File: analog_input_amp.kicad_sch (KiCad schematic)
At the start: 29 parts, among them U301 THS4521ID

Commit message: PCB: WIP Schematic: minor changes (decoupling, logic element ordering)
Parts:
- C304: value 100n -> 1u; Mfr PN CL21B104KBFNNNE -> CL21B105KOFNNNG
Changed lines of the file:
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@@
+    (pin "2")
+  )
+  (symbol (lib_id "Device:C") (at 101.6 158.75 0) (unit 1)
+    (in_bom yes) (on_board yes) (fields_autoplaced)
+    (property "Reference" "C304" (id 0) (at 104.521 157.9153 0)
+      (effects (font (size 1.27 1.27)) (justify left))
+    )
+    (property "Value" "1u" (id 1) (at 104.521 160.4522 0)
+      (effects (font (size 1.27 1.27)) (justify left))
+    )
+    (property "Footprint" "Capacitor_SMD:C_0805_2012Metric" (id 2) (at 102.5652 162.56 0)
+      (effects (font (size 1.27 1.27)) hide)
+    )
+    (property "Datasheet" "~" (id 3) (at 101.6 158.75 0)
+      (effects (font (size 1.27 1.27)) hide)
+    )
+    (property "Spec1" "" (id 4) (at 101.6 158.75 0)
+      (effects (font (size 1.27 1.27)) hide)
+    )
+    (property "Spec2" "" (id 5) (at 101.6 158.75 0)
+      (effects (font (size 1.27 1.27)) hide)
+    )
+    (property "Tolerance" "" (id 6) (at 101.6 158.75 0)
+      (effects (font (size 1.27 1.27)) hide)
+    )
+    (property "Mfr" "Samsung" (id 7) (at 101.6 158.75 0)
+      (effects (font (size 1.27 1.27)) hide)
+    )
+    (property "Mfr PN" "CL21B105KOFNNNG" (id 8) (at 101.6 158.75 0)
+      (effects (font (size 1.27 1.27)) hide)
+    )
+    (pin "1")
     (pin "2")
   )
@@
       (effects (font (size 1.27 1.27)) hide)
     )
-    (pin "1")
-    (pin "2")
-  )
-  (symbol (lib_id "Device:C") (at 101.6 158.75 0) (unit 1)
-    (in_bom yes) (on_board yes) (fields_autoplaced)
-    (property "Reference" "C304" (id 0) (at 104.521 157.9153 0)
-      (effects (font (size 1.27 1.27)) (justify left))
-    )
-    (property "Value" "100n" (id 1) (at 104.521 160.4522 0)
-      (effects (font (size 1.27 1.27)) (justify left))
-    )
-    (property "Footprint" "Capacitor_SMD:C_0805_2012Metric" (id 2) (at 102.5652 162.56 0)
-      (effects (font (size 1.27 1.27)) hide)
-    )
-    (property "Datasheet" "~" (id 3) (at 101.6 158.75 0)
-      (effects (font (size 1.27 1.27)) hide)
-    )
-    (property "Spec1" "" (id 4) (at 101.6 158.75 0)
-      (effects (font (size 1.27 1.27)) hide)
-    )
-    (property "Spec2" "" (id 5) (at 101.6 158.75 0)
-      (effects (font (size 1.27 1.27)) hide)
-    )
-    (property "Tolerance" "" (id 6) (at 101.6 158.75 0)
-      (effects (font (size 1.27 1.27)) hide)
-    )
-    (property "Mfr" "Samsung" (id 7) (at 101.6 158.75 0)
-      (effects (font (size 1.27 1.27)) hide)
-    )
-    (property "Mfr PN" "CL21B104KBFNNNE" (id 8) (at 101.6 158.75 0)
-      (effects (font (size 1.27 1.27)) hide)
-    )

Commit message: Update schematic: - Redesign of decoupling based on swcad modelling (predominantly use 1uf, no paralleled caps) - Reroute REF_CLK_IN, CLK_SEL net to different FPGA pins - Some net renaming - Ext conn: add decoupling to 3v3 output - Reassign references to all components PCB: routing almost finished
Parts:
- C301: value 1u -> 4.7u; Mfr Samsung -> Murata; Mfr PN CL21B105KOFNNNG -> GRM21BR71C475ME51
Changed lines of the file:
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@@
     (pin "1")
-  )
-  (symbol (lib_id "Device:C") (at 63.5 158.75 0) (unit 1)
-    (in_bom yes) (on_board yes) (fields_autoplaced)
-    (property "Reference" "C301" (id 0) (at 66.421 157.9153 0)
-      (effects (font (size 1.27 1.27)) (justify left))
-    )
-    (property "Value" "1u" (id 1) (at 66.421 160.4522 0)
-      (effects (font (size 1.27 1.27)) (justify left))
-    )
-    (property "Footprint" "Capacitor_SMD:C_0805_2012Metric" (id 2) (at 64.4652 162.56 0)
-      (effects (font (size 1.27 1.27)) hide)
-    )
-    (property "Datasheet" "~" (id 3) (at 63.5 158.75 0)
-      (effects (font (size 1.27 1.27)) hide)
-    )
-    (property "Spec1" "" (id 4) (at 63.5 158.75 0)
-      (effects (font (size 1.27 1.27)) hide)
-    )
-    (property "Spec2" "" (id 5) (at 63.5 158.75 0)
-      (effects (font (size 1.27 1.27)) hide)
-    )
-    (property "Tolerance" "" (id 6) (at 63.5 158.75 0)
-      (effects (font (size 1.27 1.27)) hide)
-    )
-    (property "Mfr" "Samsung" (id 7) (at 63.5 158.75 0)
-      (effects (font (size 1.27 1.27)) hide)
-    )
-    (property "Mfr PN" "CL21B105KOFNNNG" (id 8) (at 63.5 158.75 0)
-      (effects (font (size 1.27 1.27)) hide)
-    )
-    (pin "1")
-    (pin "2")
   )
   (symbol (lib_id "Device:R") (at 127 63.5 90) (unit 1)
@@
     (pin "1")
   )
+  (symbol (lib_id "Device:C") (at 63.5 158.75 0) (unit 1)
+    (in_bom yes) (on_board yes) (fields_autoplaced)
+    (property "Reference" "C301" (id 0) (at 66.421 157.9153 0)
+      (effects (font (size 1.27 1.27)) (justify left))
+    )
+    (property "Value" "4.7u" (id 1) (at 66.421 160.4522 0)
+      (effects (font (size 1.27 1.27)) (justify left))
+    )
+    (property "Footprint" "Capacitor_SMD:C_0805_2012Metric" (id 2) (at 64.4652 162.56 0)
+      (effects (font (size 1.27 1.27)) hide)
+    )
+    (property "Datasheet" "~" (id 3) (at 63.5 158.75 0)
+      (effects (font (size 1.27 1.27)) hide)
+    )
+    (property "Spec1" "" (id 4) (at 63.5 158.75 0)
+      (effects (font (size 1.27 1.27)) hide)
+    )
+    (property "Spec2" "" (id 5) (at 63.5 158.75 0)
+      (effects (font (size 1.27 1.27)) hide)
+    )
+    (property "Tolerance" "" (id 6) (at 63.5 158.75 0)
+      (effects (font (size 1.27 1.27)) hide)
+    )
+    (property "Mfr" "Murata" (id 7) (at 63.5 158.75 0)
+      (effects (font (size 1.27 1.27)) hide)
+    )
+    (property "Mfr PN" "GRM21BR71C475ME51" (id 8) (at 63.5 158.75 0)
+      (effects (font (size 1.27 1.27)) hide)
+    )
+    (pin "1")
+    (pin "2")
+  )
   (symbol (lib_id "symbols:+3.3VA") (at 63.5 152.4 0) (unit 1)

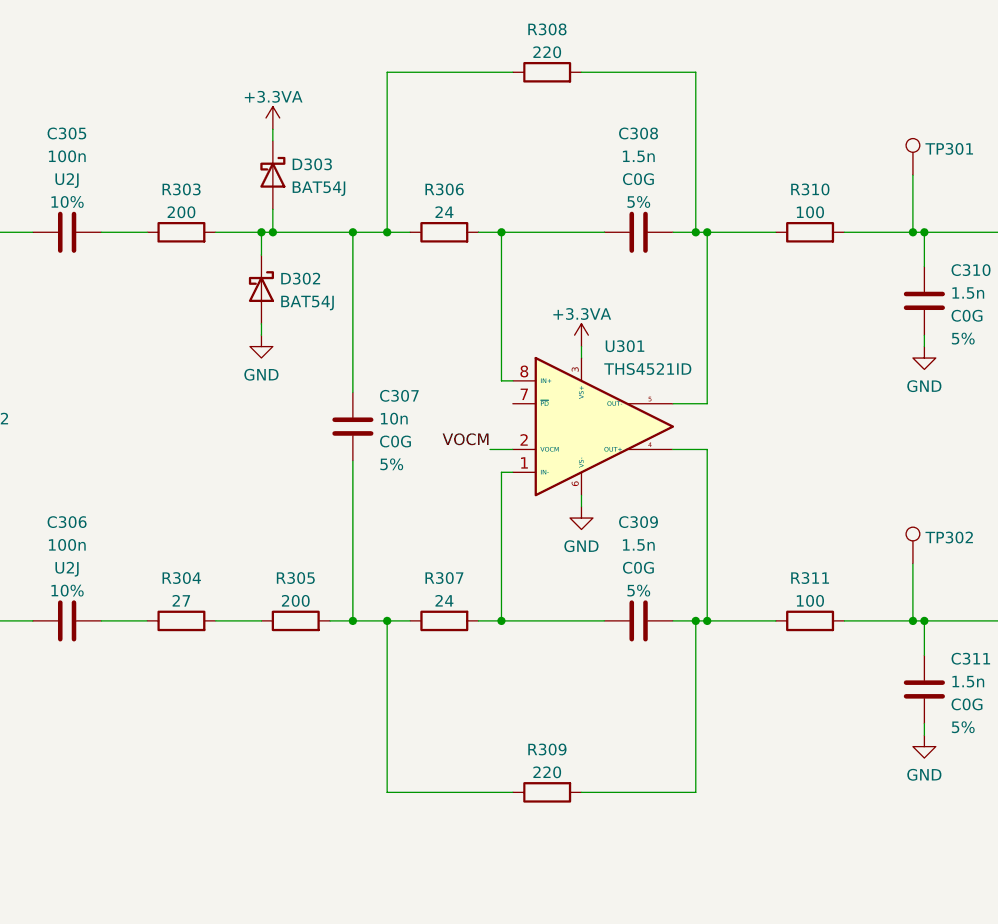
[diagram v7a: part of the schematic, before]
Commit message: Redesign FDA input overload protection
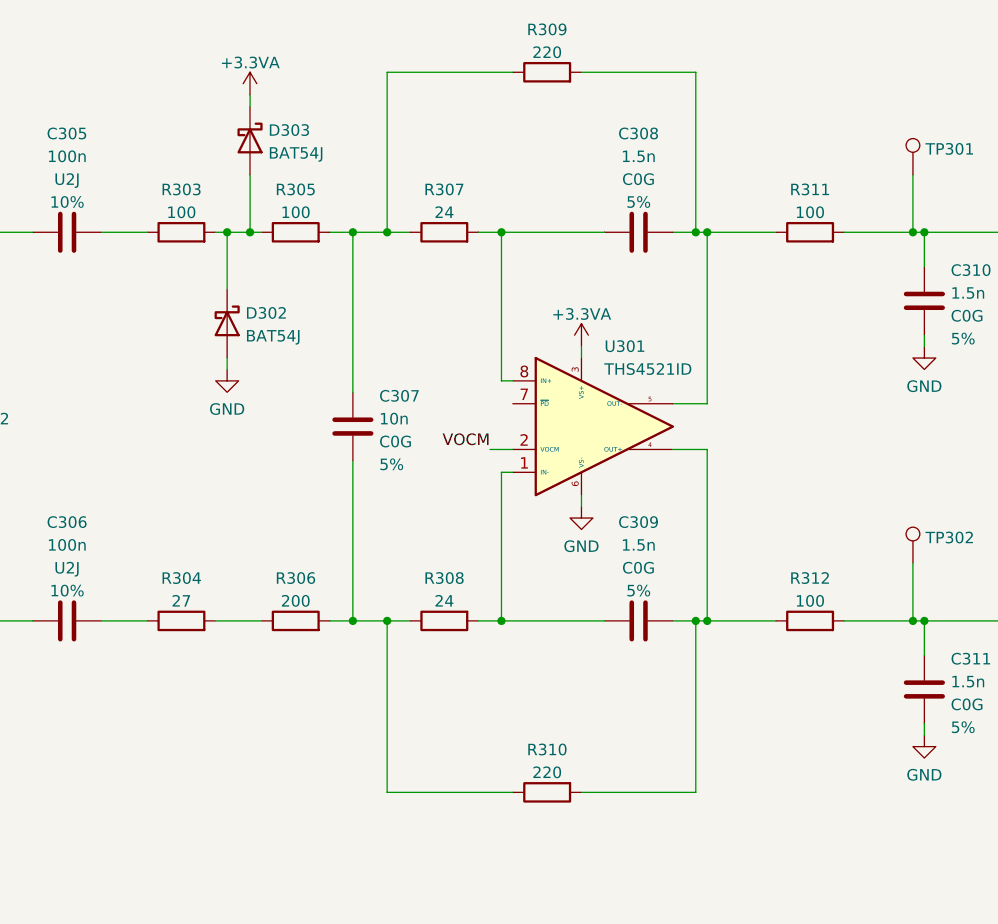
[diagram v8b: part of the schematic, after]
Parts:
- added R305: 100, Resistor_SMD:R_0805_2012Metric, symbol Device:R
- R303: value 200 -> 100; Mfr PN CR0805-FX-2000ELF -> CR0805-FX-1000ELF
- renumbered R305 to R306, R306 to R307, R307 to R308, R308 to R309, R309 to R310, R310 to R311, R311 to R312
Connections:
- net at D302.1 (K), D303.2 (A), R303.2: now also R305.1; no longer C307.2, R307.1, R309.1
- new net: C307.2, R305.2, R307.1, R309.1
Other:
- moved on the sheet: D302, D303
